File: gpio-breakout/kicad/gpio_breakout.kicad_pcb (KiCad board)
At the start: 4 copper layers, 63.5 x 32 mm, 15 parts, among them J1 FH41-40S-0.5SH(05), J2 Pi GPIO 2x20

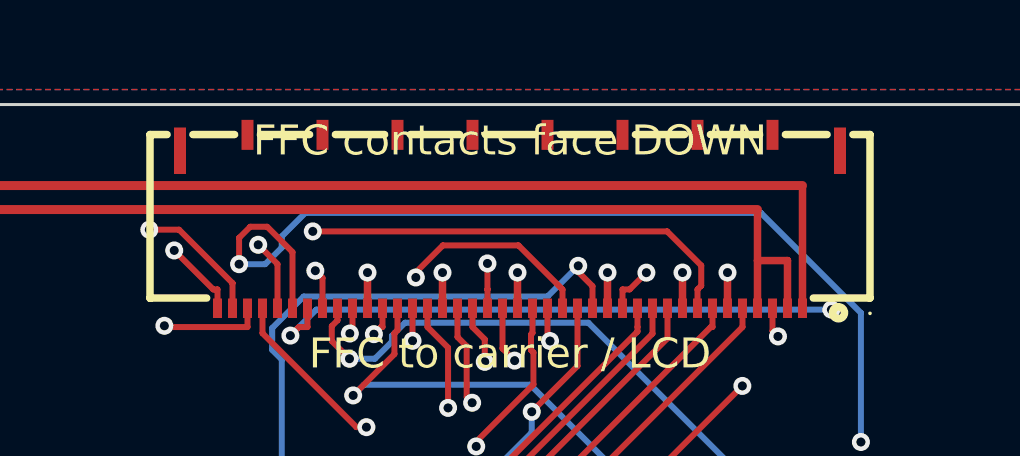
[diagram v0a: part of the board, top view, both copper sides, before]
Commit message: gpio-breakout: drop 'FFC contacts face DOWN' silk
The line printed across the FH41 connector outline. Removed from the
board and generator; gerber package + checksums + top render
regenerated. Cable contact orientation remains documented in the
README and order package notes.

Co-Authored-By: Claude Fable 5 <noreply@anthropic.com>
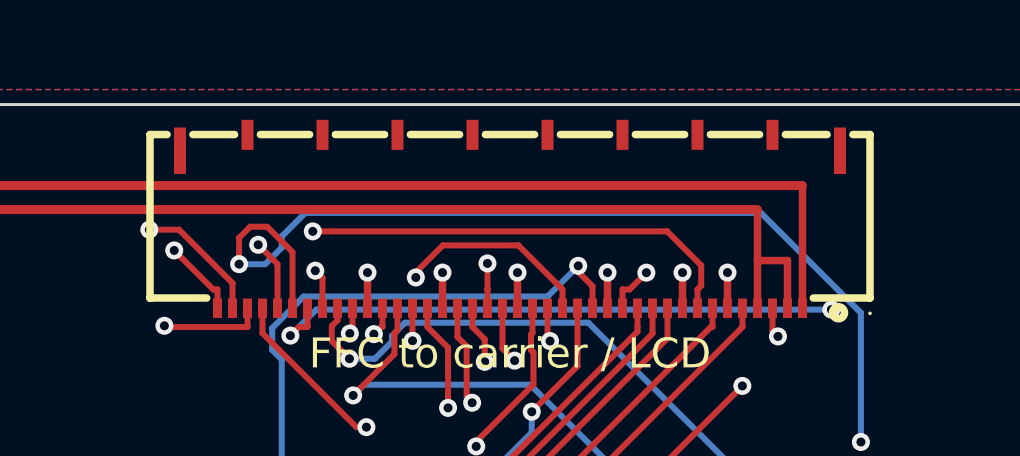
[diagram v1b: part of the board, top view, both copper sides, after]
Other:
- board text removed: "FFC contacts face DOWN"
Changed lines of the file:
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@@
-		)
-	)
-	(gr_text "FFC contacts face DOWN"
-		(at 81 51.2 0)
-		(layer "F.SilkS")
-		(effects
-			(font
-				(size 1 1)
-				(thickness 0.15)
-			)
 		)
 	)
